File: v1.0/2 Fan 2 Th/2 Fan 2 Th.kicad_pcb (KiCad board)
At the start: 2 copper layers, 55 parts, among them J1 POWER_HARNESS, J2 UPDI, J3 TH1, J4 FAN1, J5 LED_PANEL, J6 FAN2, J7 TH2, J8 BUZZER_HARNESS, Q1 AP40P05, Q2 AO3400A, Q3 AO3400A, Q4 AO3400A, U1 CJ7533S, U2 ATtiny1616-S

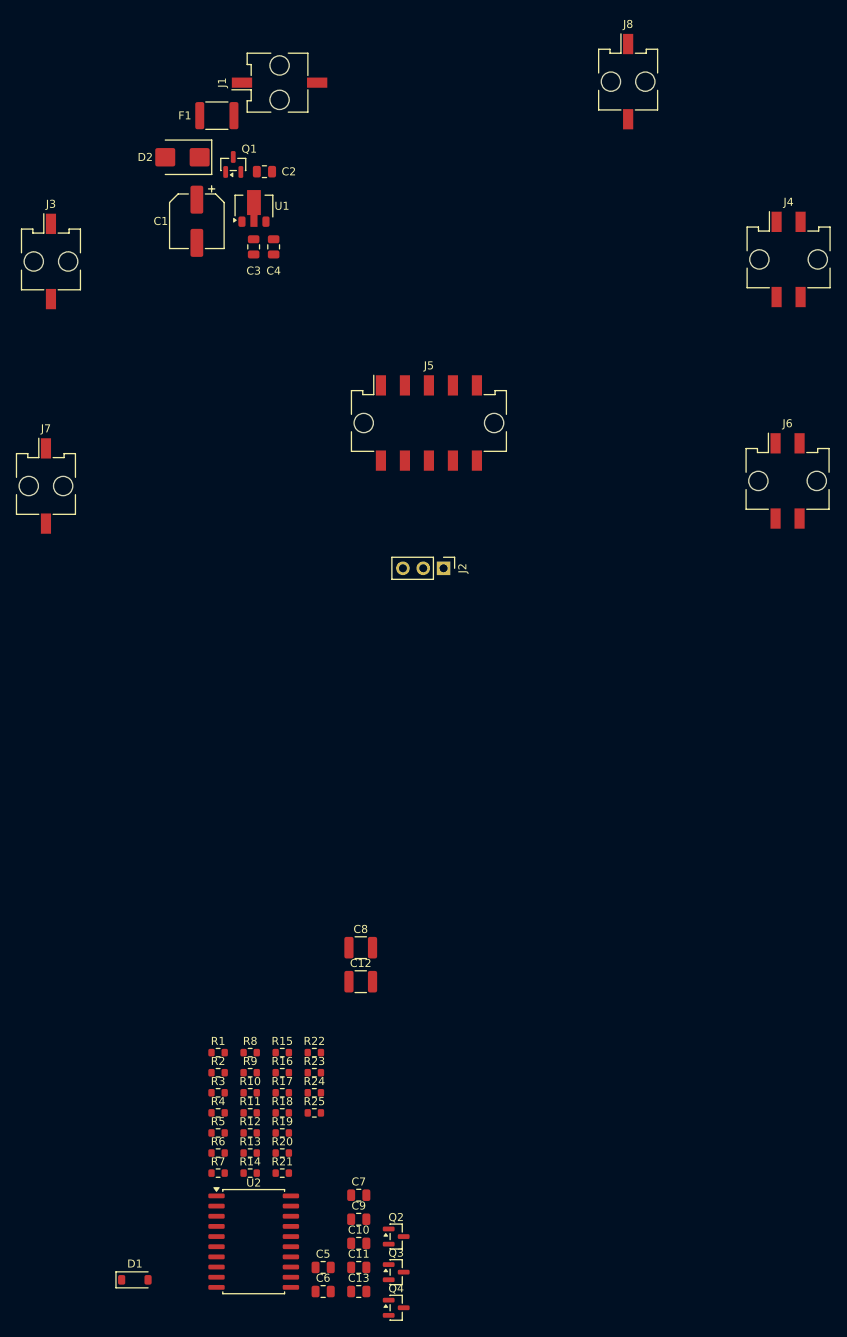
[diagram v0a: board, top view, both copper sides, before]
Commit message: design update
- silkscreen edited
- mosfet changed
- connectors type changed
- fuse changed
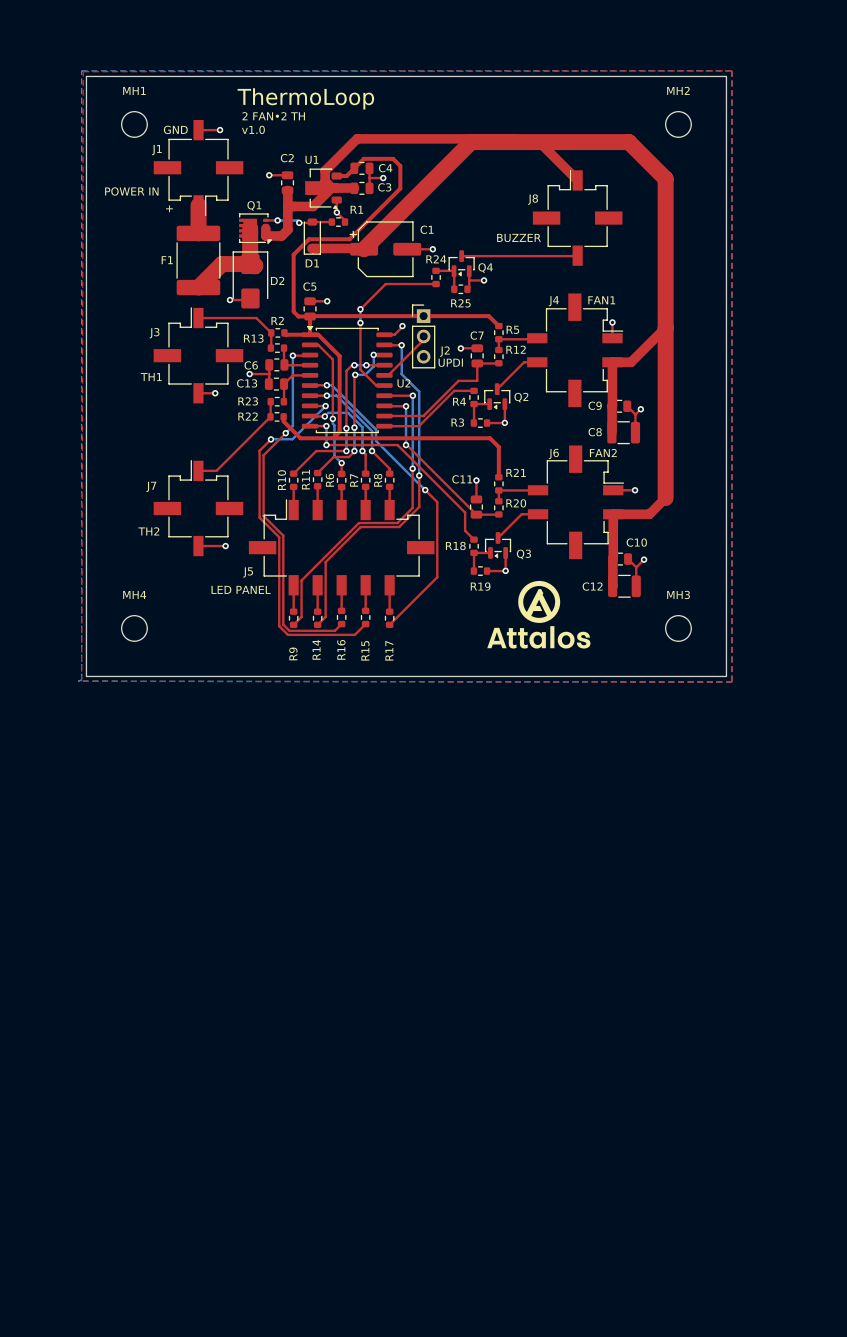
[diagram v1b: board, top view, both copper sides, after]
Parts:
- added MH1: MountingHole_3.2mm_M3, MountingHole:MountingHole_3.2mm_M3, F.Cu at (39.9, 38.5)
- added MH2: MountingHole_3.2mm_M3, MountingHole:MountingHole_3.2mm_M3, F.Cu at (107.9, 38.5)
- added MH3: MountingHole_3.2mm_M3, MountingHole:MountingHole_3.2mm_M3, F.Cu at (107.9, 101.5)
- added MH4: MountingHole_3.2mm_M3, MountingHole:MountingHole_3.2mm_M3, F.Cu at (39.9, 101.5)
- F1: value 2.5A PTC -> 2920L260/24DR; footprint Fuse:Fuse_1812_4532Metric -> Fuse:Fuse_2920_7451Metric
- J1, J3, J7, J8: footprint Connector_Molex:Molex_Micro-Fit_3.0_43045-0215_2x01_P3.00mm_Vertical -> Connector_Molex:Molex_Micro-Fit_3.0_43045-0218_2x01-1MP_P3.00mm_Vertical
- J4, J6: footprint Connector_Molex:Molex_Micro-Fit_3.0_43045-0415_2x02_P3.00mm_Vertical -> Connector_Molex:Molex_Micro-Fit_3.0_43045-0418_2x02-1MP_P3.00mm_Vertical
- J5: footprint Connector_Molex:Molex_Micro-Fit_3.0_43045-1015_2x05_P3.00mm_Vertical -> Connector_Molex:Molex_Micro-Fit_3.0_43045-1018_2x05-1MP_P3.00mm_Vertical
- Q1: value AP40P05 -> DMPH4029LFGQ; footprint Package_TO_SOT_SMD:SOT-23 -> Package_SON:Diodes_PowerDI3333-8
- moved D1 132.4 mm to (62.1, 52.4), turned to 90 degrees
- moved Q4 130.8 mm to (80.8, 55.9), turned to 90 degrees
- moved C5 119.8 mm to (61.9, 61.6), turned to 90 degrees
- moved C6 116.0 mm to (57.7, 68.6), turned to 180 degrees
- moved C13 113.9 mm to (57.6, 71.0), turned to 180 degrees
- moved U2 108.3 mm to (66.5, 70.5)
- moved C9 106.7 mm to (100.5, 73.7)
- moved R5 106.0 mm to (85.5, 64.5), turned to 90 degrees
- moved C7 106.0 mm to (82.8, 67.4), turned to 90 degrees
- moved Q2 105.7 mm to (85.2, 72.5), turned to 90 degrees
- moved R1 104.9 mm to (65.4, 50.7), turned to 180 degrees
- moved R25 104.6 mm to (80.7, 59.1)
- moved R24 103.0 mm to (77.6, 57.6), turned to 90 degrees
- moved R12 101.9 mm to (85.5, 67.5), turned to 90 degrees
- moved R13 100.7 mm to (57.8, 66.5)
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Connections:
- Q1 pad 1: Net-(D1-A) -> /VIN_PROTECTED
- Q1 pad 3: /VIN_FUSED -> /VIN_PROTECTED
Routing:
- net /VIN_PROTECTED: track 0.00 -> 178.8 mm
- net +3V3: track 0.00 -> 115.8 mm
- net GND: track 0.00 -> 66.4 mm, vias 0 -> 20
- net /FAN2_LED_B_CTRL: track 0.00 -> 47.3 mm, vias 0 -> 2
- net /TH1_LED_B_CTRL: track 0.00 -> 46.3 mm, vias 0 -> 2
- net /FAN1_LED_B_CTRL: track 0.00 -> 46.1 mm, vias 0 -> 2
- net /SYSTEM_LED_B_CTRL: track 0.00 -> 41.2 mm, vias 0 -> 2
- net /TH2_LED_B_CTRL: track 0.00 -> 40.6 mm, vias 0 -> 2
- net /FAN2_PWM_CTRL: track 0.00 -> 29.1 mm, vias 0 -> 2
- net /SYSTEM_LED_A_CTRL: track 0.00 -> 22.8 mm, vias 0 -> 4
- net /FAN2_TACH: track 0.00 -> 22.8 mm, vias 0 -> 2
- net /BUZZER_CTRL: track 0.00 -> 22.1 mm, vias 0 -> 2
- net /FAN1_LED_A_CTRL: track 0.00 -> 20.9 mm, vias 0 -> 4
- net /TH1_LED_A_CTRL: track 0.00 -> 18.4 mm, vias 0 -> 2
- net /FAN1_TACH: track 0.00 -> 18.3 mm
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- added copper zone on B.Cu, net GND
- added copper zone on F.Cu, net GND
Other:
- board outline added: 80 x 75 mm
- board text added: "+"
- board text added: "2 FAN•2 TH"
- board text added: "BUZZER"
- board text added: "FAN1"
- board text added: "FAN2"
- board text added: "GND"
- board text added: "LED PANEL"
- board text added: "POWER IN"
- board text added: "TH1"
- board text added: "TH2"
- board text added: "ThermoLoop"
- board text added: "UPDI"
- board text added: "v1.0"

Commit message: F2Th2 Finalized
F2Th2 finalized
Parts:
- C1: value 100uF 35V -> 100 µF 35V
- C13, C5, C6: value 100 nF 50V -> 100 nF 50 V
- C2: value 100nF 50V -> 100 nF 50 V
- C3, C4: value 1uF 50V -> 1 µF 50 V
- U2: value ATtiny1616-S -> ATTINY1616-SNR
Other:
- board text added: "+VIN"
- board text added: "3V3"
- board text added: "A 1 SYS 2 FAN1 3 TH1 4 FAN2 5 TH2"
- board text added: "B 6 SYS 7 FAN1 8 TH1 9 FAN2 10 TH2"
- board text added: "PROG"
- board text added: "PWM"
- board text added: "SW"
- board text added: "TACH"
- board text added: "VIN"
- board text added: "v1.0 09-2026"
- board text removed: "+"
- board text removed: "v1.0"

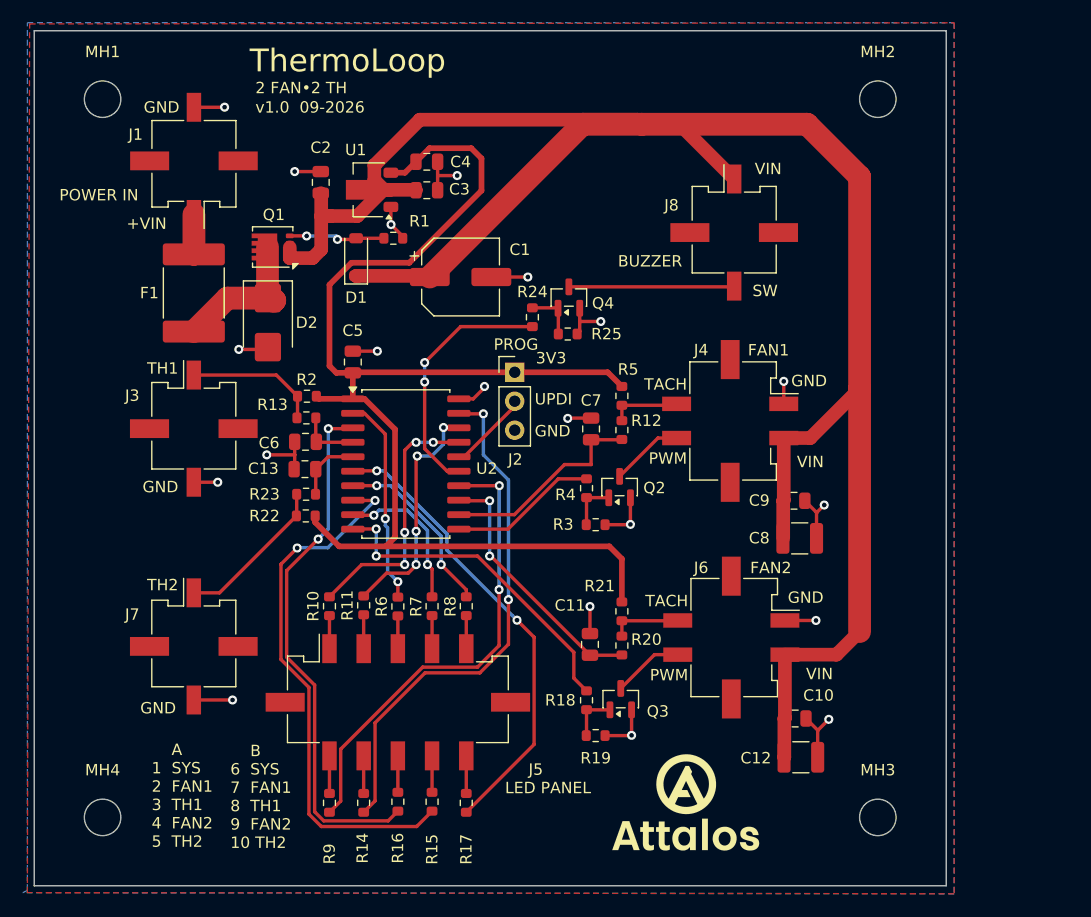
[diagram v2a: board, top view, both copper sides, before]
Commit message: simulations & silkscreen edits
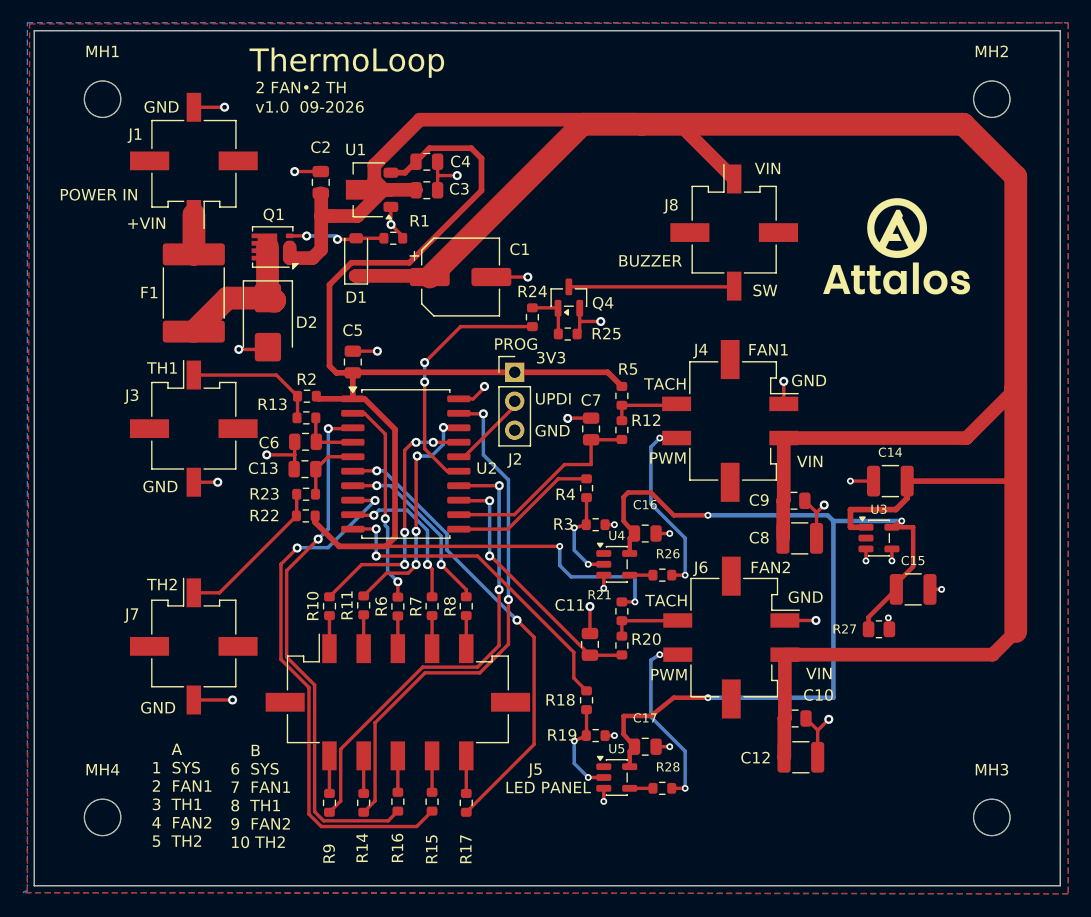
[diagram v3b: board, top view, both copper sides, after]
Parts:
- removed Q2, Q3: AO3400A, Package_TO_SOT_SMD:SOT-23
- added C14: 10 µF 50 V, Capacitor_SMD:C_1210_3225Metric, F.Cu at (109.0, 72.0)
- added C15: 10 µF 50 V, Capacitor_SMD:C_1210_3225Metric, F.Cu at (111.0, 81.5)
- added C16: 100 nF 50 V, Capacitor_SMD:C_0805_2012Metric, F.Cu at (87.5, 76.6)
- added C17: 100 nF 50 V, Capacitor_SMD:C_0805_2012Metric, F.Cu at (87.5, 95.3)
- added R26: 33 Ω, Resistor_SMD:R_0603_1608Metric, F.Cu at (89.0, 80.2)
- added R27: 330 Ω, Resistor_SMD:R_0805_2012Metric, F.Cu at (108.0, 85.0)
- added R28: 33 Ω, Resistor_SMD:R_0603_1608Metric, F.Cu at (89.0, 99.0)
- added U3: TPS7B6950QDBVRQ1, Package_TO_SOT_SMD:SOT-23-5, F.Cu at (108.0, 77.0)
- added U4: SN74AHCT1G04DBVR, Package_TO_SOT_SMD:SOT-23-5, F.Cu at (85.0, 79.3)
- added U5: SN74AHCT1G04DBVR, Package_TO_SOT_SMD:SOT-23-5, F.Cu at (85.0, 98.0)
- R10, R11, R14, R15, R16, R17, R6, R7, R8, R9: value 220 Ω -> 150 Ω
- moved MH2 10.0 mm to (117.9, 38.5)
- moved MH3 10.0 mm to (117.9, 101.5)
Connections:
- net Net-(Q2-G) renamed /FAN1_PWM_IN
- net Net-(Q3-G) renamed /FAN2_PWM_IN
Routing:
- net /+5V_PWM: track 0.00 -> 84.0 mm, vias 0 -> 3
- net /VIN_PROTECTED: track 178.8 -> 239.2 mm
- net /FAN2_PWM: track 6.23 -> 16.2 mm, vias 0 -> 2
- net /FAN1_PWM: track 6.39 -> 16.2 mm, vias 0 -> 2
- net /FAN1_PWM_IN: track 4.34 -> 8.53 mm, vias 0 -> 2
- net /FAN2_PWM_IN: track 4.34 -> 8.50 mm, vias 0 -> 2
- net GND: track 66.4 -> 69.7 mm, vias 20 -> 29
- net +3V3: track 115.8 -> 118.2 mm, vias 0 -> 2
- net /FAN2_PWM_DRIVE: track 0.00 -> 2.04 mm
- net /FAN1_PWM_DRIVE: track 0.00 -> 2.04 mm
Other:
- board size 80 x 75 mm -> 90 x 75 mm
